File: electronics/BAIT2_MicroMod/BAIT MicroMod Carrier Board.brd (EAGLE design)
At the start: 92.7 x 80 mm, 159 parts, among them J1 SJ-43516-SMT, J10 QWIIC_RIGHT_ANGLE, J11 QWIIC_RIGHT_ANGLE, J15 BM05B-SRSS-TB(LF)(SN), J2 ST-TF-003A, J4 BM05B-SRSS-TB(LF)(SN), J5 QWIIC_RIGHT_ANGLE, J6 JST 2PH, J7 MICROMOD-2222-C, SW1 SKQGADE010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

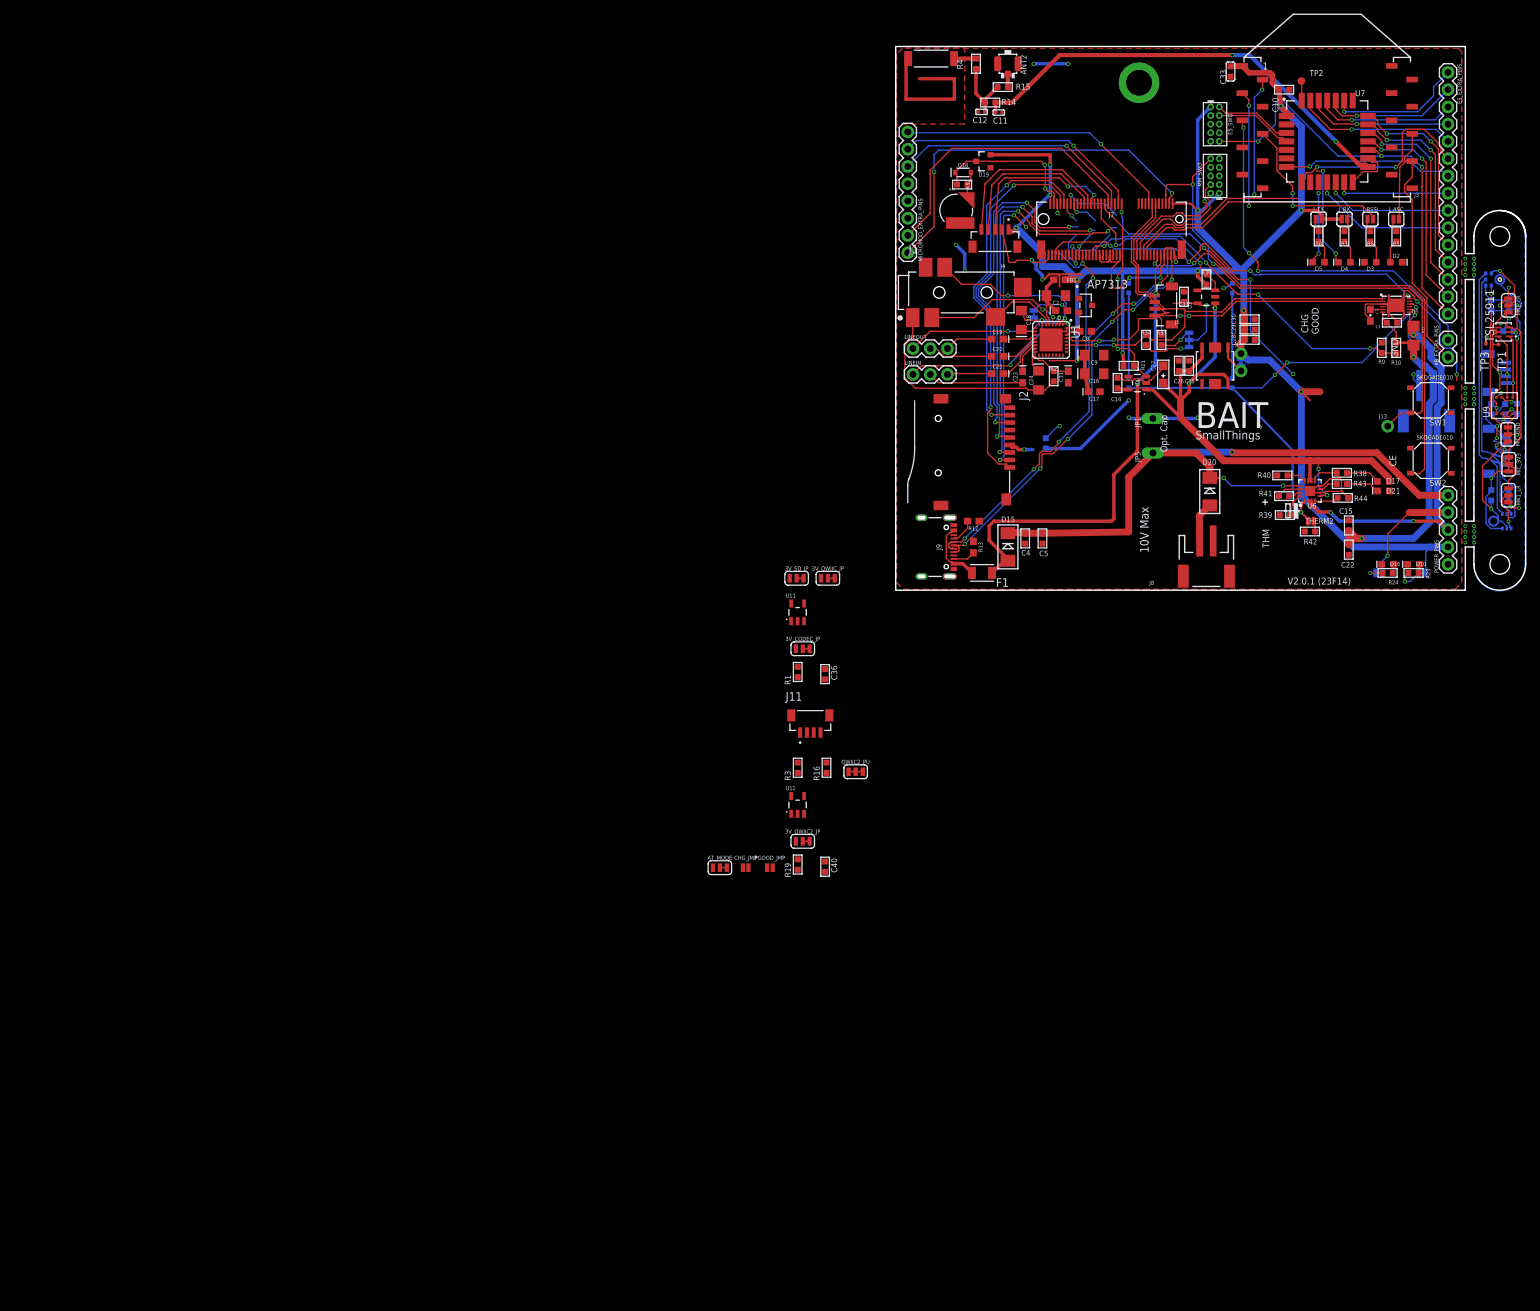
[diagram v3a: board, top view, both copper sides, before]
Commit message: Updated layout for TC2956 chip
Should resolve #29, but I should double check
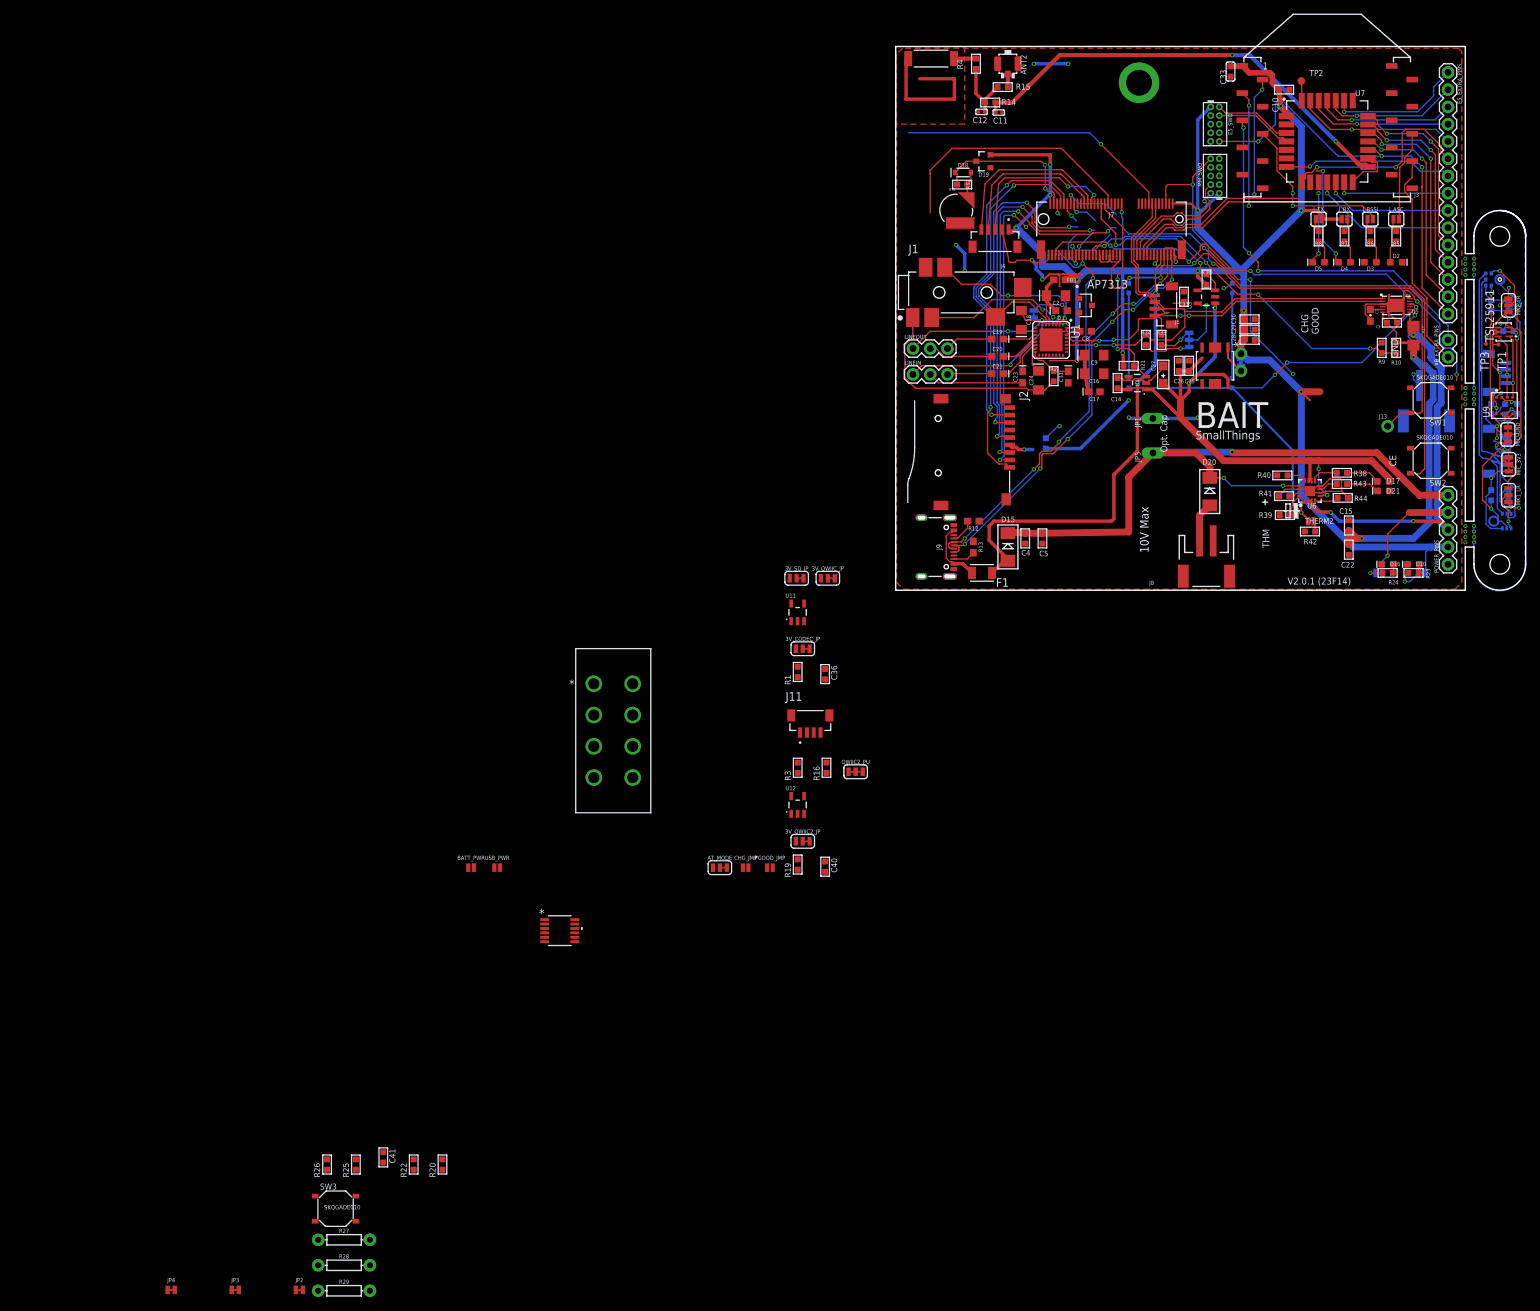
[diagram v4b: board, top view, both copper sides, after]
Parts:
- removed MICROMOD_EXTRA_PINS: (no value), SparkFun-Connectors:1X08
- added BATT_PWR, USB_PWR: (no value), SparkFun-Jumpers:SMT-JUMPER_2_NO_NO-SILK
- added C41: 100nf, OPL_Capacitor:C0603
- added J12: L203011MS02QECONN8_MS02QE_CNK, BAIT-Components:CONN8_MS02QE_CNK
- added JP2, JP3, JP4: JUMPER-SMT_2_NC_TRACE_NO-SILK, SparkFun-Jumpers:SMT-JUMPER_2_NC_TRACE_NO-SILK
- added R20: 100K, OPL_Resistor:R0603
- added R22: 1.02M, OPL_Resistor:R0603
- added R25: 61.9k, OPL_Resistor:R0603
- added R26: 115k, OPL_Resistor:R0603
- added R27, R28, R29: (no value), SparkFun-Resistors:AXIAL-0.3
- added SW3: SKQGADE010, OPL_Switch:SW4-SMD-5.2X5.2X1.5MM
- added U13: LTC2956IMS-1PBF, BAIT-Components:MSOP-12_MS_LIT
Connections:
- removed net 3.3V_EN: J7.4, MICROMOD_EXTRA_PINS.1
- removed net A0: J7.34, MICROMOD_EXTRA_PINS.7
- removed net A1: J7.38, MICROMOD_EXTRA_PINS.6
- new net !OFFALERT!: J7.38, U13.10
- new net !ONALERT!: J7.34, U13.12
- new net !PB: SW3.2, U13.7
- new net !PBOUT!: J7.65, U13.9
- new net !SLEEP!: J7.8, U13.11
- new net 3V_EN: U13.8, U8.3
- new net N$77: U3.5
- new net N$78: JP3.2, R20.2, R28.P$2, U13.3
- new net N$79: JP2.1, R22.2
- new net N$80: JP4.2, R29.P$2, U13.4
- new net N$81: JP2.2, R20.1, R27.P$2, U13.2
- new net N$82: JP3.1, R25.2
- new net N$83: JP4.1, R26.2
- new net V_BATT_IN: BATT_PWR.2, J12.6, J6.1
- new net V_USB_IN: D15.C, J12.2, USB_PWR.2
- net 3V_QWIIC_OUT: no longer U3.5
- net GND: now also C41.2, R22.1, R25.1, R26.1, R27.P$1, R28.P$1, R29.P$1, SW3.4, U13.1, U13.6
- net HEADER_!CS!: no longer MICROMOD_EXTRA_PINS.2
- net I2C_!INT!: no longer MICROMOD_EXTRA_PINS.8
- net V+: now also C41.1, U13.5; no longer U8.3
- net VBUS: now also J12.1, J12.3, USB_PWR.1; no longer D15.C
- net VIN: now also BATT_PWR.1, J12.5, J12.7; no longer J6.1
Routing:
- net 3.3V_EN: track 55.6 -> 0.00 mm, vias 2 -> 0
- net A0: track 36.5 -> 0.00 mm, vias 1 -> 0
- net A1: track 35.9 -> 0.00 mm, vias 1 -> 0
- net HEADER_!CS!: track 42.6 -> 37.9 mm
- net VIN: track 60.6 -> 56.8 mm
- net 3V_QWIIC_OUT: track 3.81 -> 1.91 mm
- net V+: track 107.5 -> 106.0 mm

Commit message: Fixed headphone jack detection
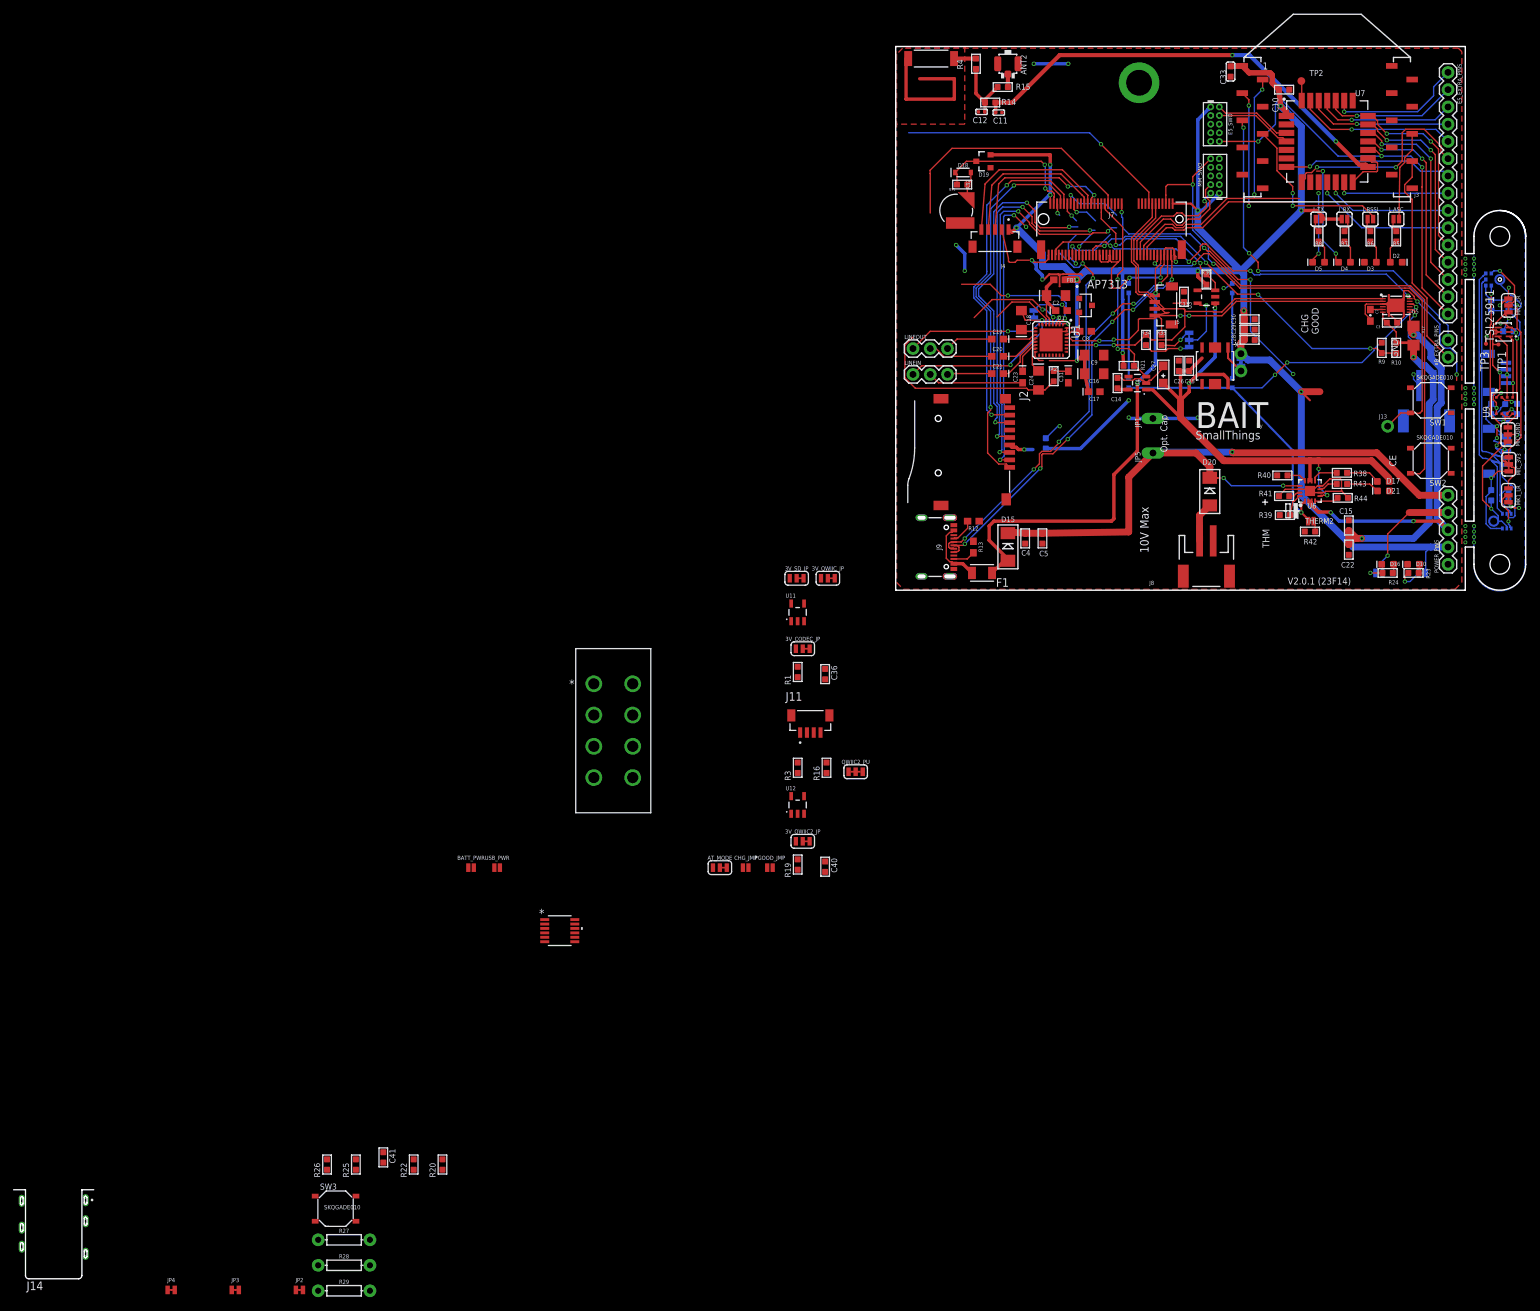
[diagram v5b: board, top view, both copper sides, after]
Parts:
- removed J1: SJ-43516-SMT, SnapEDA-Library:CUI_SJ-43516-SMT
- added J14: SJ-3551B-MSMT-TR-67, BAIT-Components:CUI_SJ-3551B-MSMT-TR-67
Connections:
- removed net HP_RING_SW_NC: J1.6, J7.69
- removed net HP_TIP_SW_NC: J1.5, J7.67
- new net HP_DETECT: J14.5, J7.69
- net GND: now also J14.6
- net N$33: now also J14.1; no longer J1.1
- net N$35: now also J14.3; no longer J1.3
- net N$48: now also J14.4; no longer J1.4
- net N$8: now also J14.2; no longer J1.2
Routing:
- net N$48: track 21.2 -> 14.9 mm
- net N$35: track 23.7 -> 20.2 mm
- net N$33: track 32.5 -> 29.6 mm
- net N$84: track 6.53 -> 4.35 mm
